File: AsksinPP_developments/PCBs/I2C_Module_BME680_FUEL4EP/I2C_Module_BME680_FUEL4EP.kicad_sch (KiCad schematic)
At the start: 12 parts, among them J1 Conn_01x04, J2 Conn_01x04, U1 BME680

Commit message: PCBs: I2C_Module_BME280_FUEL4EP and I2C_Module_BME680_FUEL4EP: updated LCSC numberss for assembly at JLCPCB
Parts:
- C1: LCSC (none) -> C19666; TYPE (none) -> 0603
- C3, C4: LCSC (none) -> C14663; TYPE (none) -> 0603
- R1, R2: LCSC (none) -> C25900; TYPE (none) -> 0402
- R3: LCSC (none) -> C25744; TYPE (none) -> 0402
- U1: LCSC (none) -> C125972; TYPE (none) -> LGA-8
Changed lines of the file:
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@@
       (effects (font (size 1.27 1.27)) hide)
+    )
+    (property "LCSC" "C25900" (id 4) (at 147.955 123.19 0)
+      (effects (font (size 1.27 1.27)) hide)
+    )
+    (property "TYPE" "0402" (id 5) (at 151.765 120.65 0)
+      (effects (font (size 1.524 1.524)) hide)
     )
     (pin "1")
@@
       (effects (font (size 1.27 1.27)) hide)
     )
+    (property "LCSC" "C14663" (id 4) (at 132.715 56.515 0)
+      (effects (font (size 1.27 1.27)) hide)
+    )
+    (property "TYPE" "0603" (id 5) (at 137.795 54.61 0)
+      (effects (font (size 1.524 1.524)) hide)
+    )
     (pin "1")
     (pin "2")
@@
     (property "Datasheet" "~" (id 3) (at 173.355 55.88 0)
       (effects (font (size 1.27 1.27)) hide)
+    )
+    (property "LCSC" "C25744" (id 4) (at 169.545 59.69 0)
+      (effects (font (size 1.27 1.27)) hide)
+    )
+    (property "TYPE" "0402" (id 5) (at 173.355 55.88 0)
+      (effects (font (size 1.524 1.524)) hide)
     )
     (pin "1")
@@
       (effects (font (size 1.27 1.27)) hide)
     )
+    (property "LCSC" "C19666" (id 4) (at 75.438 128.27 0)
+      (effects (font (size 1.27 1.27)) hide)
+    )
+    (property "TYPE" "0603" (id 5) (at 79.375 130.175 90)
+      (effects (font (size 1.524 1.524)) hide)
+    )
     (pin "1")
     (pin "2")
@@
     (property "Datasheet" "~" (id 3) (at 121.285 54.61 0)
       (effects (font (size 1.27 1.27)) hide)
+    )
+    (property "LCSC" "C14663" (id 4) (at 116.205 56.515 0)
+      (effects (font (size 1.27 1.27)) hide)
+    )
+    (property "TYPE" "0603" (id 5) (at 121.285 54.61 0)
+      (effects (font (size 1.524 1.524)) hide)
     )
     (pin "1")
@@
     (property "Datasheet" "https://ae-bst.resource.bosch.com/media/_tech/media/datasheets/BST-BME680-DS001.pdf" (id 3) (at 130.175 87.63 0)
       (effects (font (size 1.27 1.27)) hide)
+    )
+    (property "LCSC" "C125972" (id 4) (at 130.175 82.55 0)
+      (effects (font (size 1.524 1.524)) hide)
+    )
+    (property "TYPE" "LGA-8" (id 5) (at 130.175 82.55 0)
+      (effects (font (size 1.524 1.524)) hide)
     )
     (pin "1")
@@
       (effects (font (size 1.27 1.27)) hide)
     )
-    (pin "1")
+    (property "LCSC" "C25900" (id 4) (at 154.305 123.19 0)
+      (effects (font (size 1.27 1.27)) hide)
+    )
+    (property "TYPE" "0402" (id 5) (at 158.115 120.65 0)
+      (effects (font (size 1.524 1.524)) hide)
+    )
+    (pin "1")

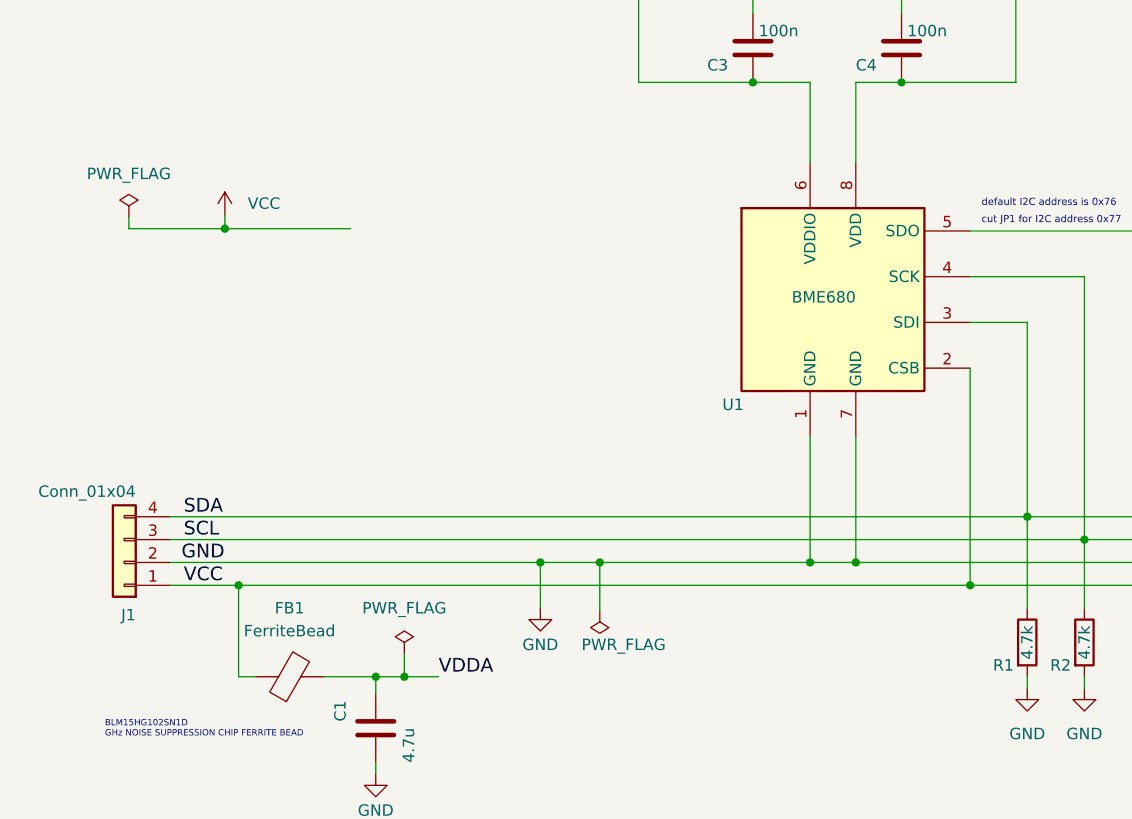
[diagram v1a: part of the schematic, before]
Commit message: PCBs: fix of some project specific KiCAD library paths for portability and missing PWR_FLGs for VCC in some schematics
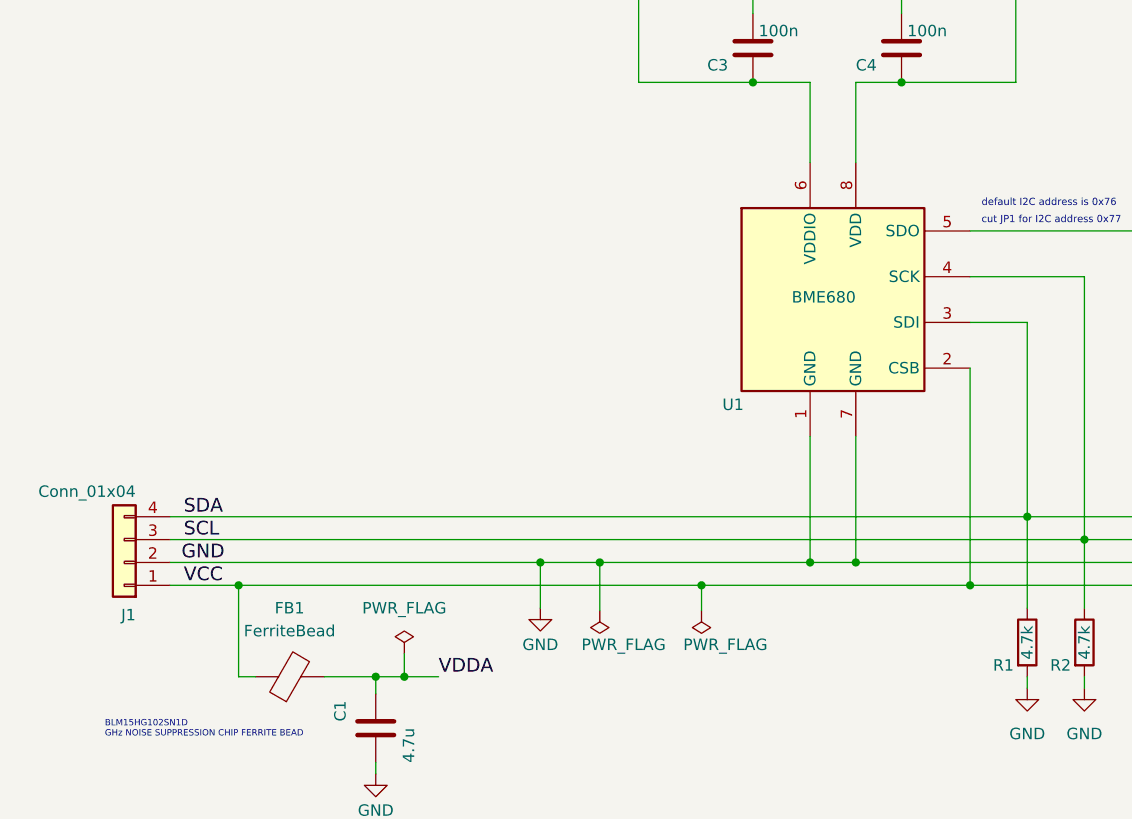
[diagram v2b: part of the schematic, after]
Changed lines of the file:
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@@
   (title_block
     (title "I2C_Module_BME680_FUEL4EP")
-    (date "2023-09-07")
-    (rev "1.0")
+    (date "2024-01-14")
+    (rev "1.1")
     (company "FUEL4EP")
     (comment 1 "fitting to  HB-UNI-SEN-BATT_ATMega1284P_E07-868MS10_FUEL4EP")
@@
   (junction (at 132.715 111.76) (diameter 0) (color 0 0 0 0)
   )
-  (junction (at 62.611 74.676) (diameter 0) (color 0 0 0 0)
-  )
   (junction (at 137.795 58.42) (diameter 0) (color 0 0 0 0)
   )
@@
   (junction (at 82.55 124.46) (diameter 0) (color 0 0 0 0)
   )
+  (junction (at 115.57 114.3) (diameter 0) (color 0 0 0 0)
+  )
   (junction (at 173.355 74.93) (diameter 0) (color 0 0 0 0)
   )
@@
     (stroke (width 0) (type default) (color 0 0 0 0))
   )
-  (wire (pts (xy 51.943 74.676) (xy 51.943 73.406))
-    (stroke (width 0) (type default) (color 0 0 0 0))
-  )
   (wire (pts (xy 121.285 48.26) (xy 121.285 50.8))
     (stroke (width 0) (type default) (color 0 0 0 0))
@@
     (stroke (width 0) (type default) (color 0 0 0 0))
   )
-  (wire (pts (xy 62.611 74.676) (xy 51.943 74.676))
-    (stroke (width 0) (type default) (color 0 0 0 0))
-  )
   (wire (pts (xy 145.415 80.01) (xy 158.115 80.01))
     (stroke (width 0) (type default) (color 0 0 0 0))
@@
     (stroke (width 0) (type default) (color 0 0 0 0))
   )
+  (wire (pts (xy 115.57 114.3) (xy 115.57 117.094))
+    (stroke (width 0) (type default) (color 0 0 0 0))
+  )
   (wire (pts (xy 79.375 124.46) (xy 79.375 126.365))
     (stroke (width 0) (type default) (color 0 0 0 0))
@@
     (stroke (width 0) (type default) (color 0 0 0 0))
   )
-  (wire (pts (xy 62.611 74.676) (xy 62.611 73.152))
-    (stroke (width 0) (type default) (color 0 0 0 0))
-  )
   (wire (pts (xy 108.585 58.42) (xy 121.285 58.42))
     (stroke (width 0) (type default) (color 0 0 0 0))
   )
-  (wire (pts (xy 64.135 114.3) (xy 145.415 114.3))
+  (wire (pts (xy 64.135 114.3) (xy 115.57 114.3))
     (stroke (width 0) (type default) (color 0 0 0 0))
   )
@@
     (stroke (width 0) (type default) (color 0 0 0 0))
   )
-  (wire (pts (xy 62.611 74.676) (xy 76.581 74.676))
-    (stroke (width 0) (type default) (color 0 0 0 0))
-  )
   (wire (pts (xy 56.515 111.76) (xy 97.663 111.76))
     (stroke (width 0) (type default) (color 0 0 0 0))
   )
   (wire (pts (xy 104.267 111.76) (xy 127.635 111.76))
+    (stroke (width 0) (type default) (color 0 0 0 0))
+  )
+  (wire (pts (xy 115.57 114.3) (xy 145.415 114.3))
     (stroke (width 0) (type default) (color 0 0 0 0))
   )
@@
     (pin "1")
   )
+  (symbol (lib_id "power:PWR_FLAG") (at 115.57 117.094 180) (unit 1)
+    (in_bom yes) (on_board yes)
+    (property "Reference" "#FLG0102" (id 0) (at 115.57 118.999 0)
+      (effects (font (size 1.27 1.27)) hide)
+    )
+    (property "Value" "PWR_FLAG" (id 1) (at 113.538 120.904 0)
+      (effects (font (size 1.27 1.27)) (justify right))
+    )
+    (property "Footprint" "" (id 2) (at 115.57 117.094 0)
+      (effects (font (size 1.27 1.27)) hide)
+    )
+    (property "Datasheet" "~" (id 3) (at 115.57 117.094 0)
+      (effects (font (size 1.27 1.27)) hide)
+    )
+    (pin "1")
+  )
   (symbol (lib_id "Device:R") (at 173.355 55.88 0) (unit 1)
     (in_bom yes) (on_board yes)
@@
     (pin "1")
     (pin "2")
-  )
-  (symbol (lib_id "power:VCC") (at 62.611 73.152 0) (unit 1)
-    (in_bom yes) (on_board yes) (fields_autoplaced)
-    (property "Reference" "#PWR01" (id 0) (at 62.611 76.962 0)
-      (effects (font (size 1.27 1.27)) hide)
-    )
-    (property "Value" "VCC" (id 1) (at 65.151 71.8819 0)
-      (effects (font (size 1.27 1.27)) (justify left))
-    )
-    (property "Footprint" "" (id 2) (at 62.611 73.152 0)
-      (effects (font (size 1.27 1.27)) hide)
-    )
-    (property "Datasheet" "" (id 3) (at 62.611 73.152 0)
-      (effects (font (size 1.27 1.27)) hide)
-    )
-    (pin "1")
   )
   (symbol (lib_id "Device:C") (at 79.375 130.175 0) (unit 1)
@@
     )
     (property "Datasheet" "" (id 3) (at 79.375 135.255 0)
-      (effects (font (size 1.27 1.27)) hide)
-    )
-    (pin "1")
-  )
-  (symbol (lib_id "power:PWR_FLAG") (at 51.943 73.406 0) (unit 1)
-    (in_bom yes) (on_board yes) (fields_autoplaced)
-    (property "Reference" "#FLG01" (id 0) (at 51.943 71.501 0)
-      (effects (font (size 1.27 1.27)) hide)
-    )
-    (property "Value" "PWR_FLAG" (id 1) (at 51.943 68.58 0))
-    (property "Footprint" "" (id 2) (at 51.943 73.406 0)
-      (effects (font (size 1.27 1.27)) hide)
-    )
-    (property "Datasheet" "~" (id 3) (at 51.943 73.406 0)
       (effects (font (size 1.27 1.27)) hide)
     )
@@
   )
   (symbol_instances
-    (path "/accbd0c3-e588-4a03-8c25-5dc64064deb9"
-      (reference "#FLG01") (unit 1) (value "PWR_FLAG") (footprint "")
-    )
     (path "/b998681a-aa50-4b75-bf22-d9fbe42fce6f"
       (reference "#FLG02") (unit 1) (value "PWR_FLAG") (footprint "")
@@
       (reference "#FLG0101") (unit 1) (value "PWR_FLAG") (footprint "")
     )
-    (path "/71fc455e-be46-44e1-9ad6-6659dc653656"
-      (reference "#PWR01") (unit 1) (value "VCC") (footprint "")
+    (path "/538d4725-6508-47aa-bf0f-3fed7444df70"
+      (reference "#FLG0102") (unit 1) (value "PWR_FLAG") (footprint "")
     )
     (path "/2fb280af-9352-43f7-93d8-89326fb5dc6f"

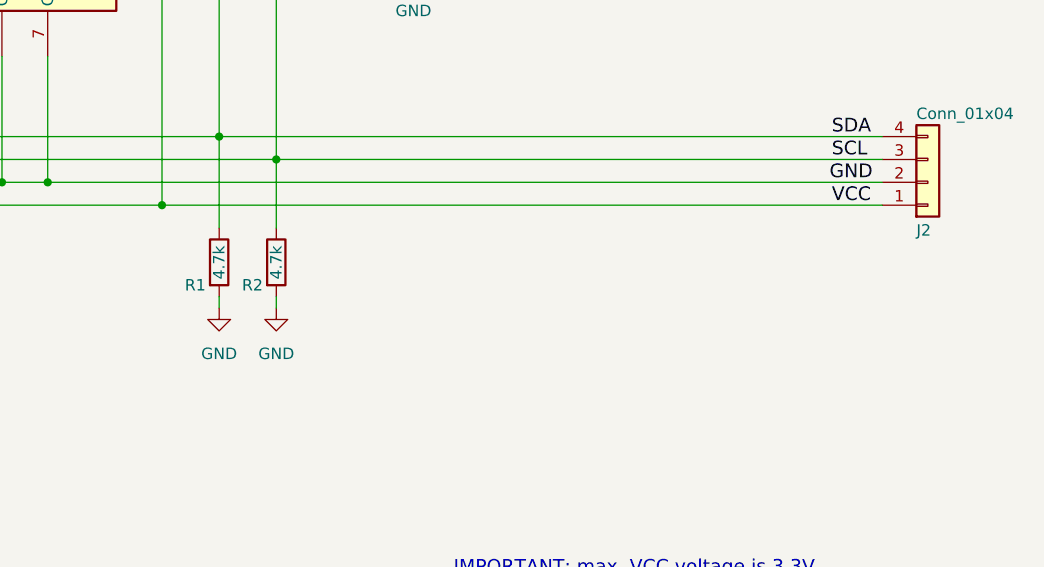
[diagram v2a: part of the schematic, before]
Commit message: PCBs: fix of I2C Pull-up resistors that were wrongly tied to GND
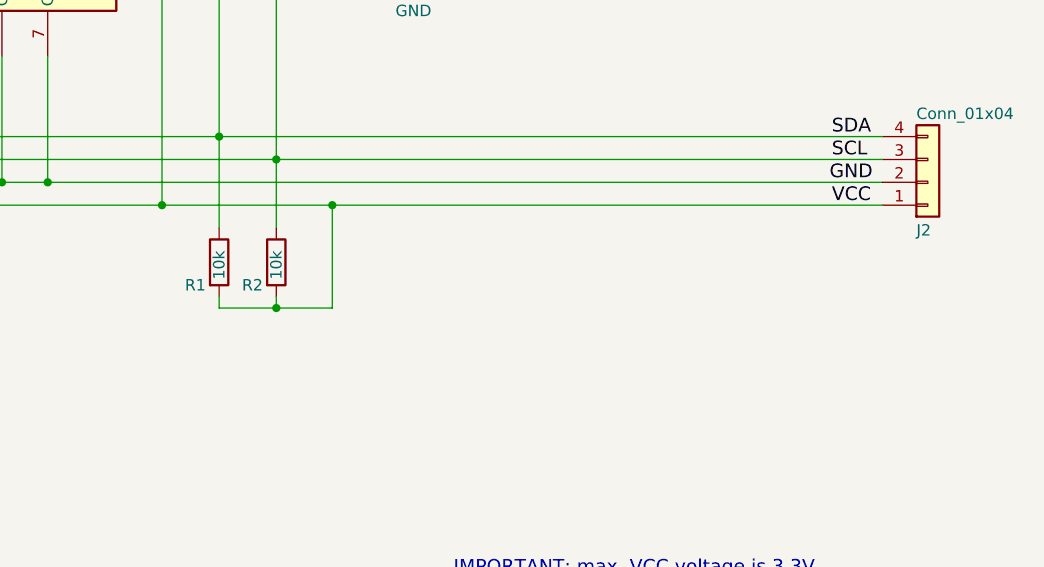
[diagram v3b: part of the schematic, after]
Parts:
- R1, R2: value 4.7k -> 10k; LCSC C25900 -> C25744
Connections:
- net GND: no longer R1.2, R2.2
- net VCC: now also R1.2, R2.2
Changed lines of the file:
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@@
   (title_block
     (title "I2C_Module_BME680_FUEL4EP")
-    (date "2024-01-14")
-    (rev "1.1")
+    (date "2024-02-08")
+    (rev "1.2")
     (company "FUEL4EP")
     (comment 1 "fitting to  HB-UNI-SEN-BATT_ATMega1284P_E07-868MS10_FUEL4EP")
@@
   (junction (at 137.795 58.42) (diameter 0) (color 0 0 0 0)
   )
+  (junction (at 164.338 114.3) (diameter 0) (color 0 0 0 0)
+  )
   (junction (at 79.375 124.46) (diameter 0) (color 0 0 0 0)
   )
   (junction (at 121.285 58.42) (diameter 0) (color 0 0 0 0)
   )
+  (junction (at 158.115 125.73) (diameter 0) (color 0 0 0 0)
+  )
   (junction (at 97.663 111.76) (diameter 0) (color 0 0 0 0)
   )
@@
     (stroke (width 0) (type default) (color 0 0 0 0))
   )
+  (wire (pts (xy 132.715 58.42) (xy 137.795 58.42))
+    (stroke (width 0) (type default) (color 0 0 0 0))
+  )
+  (wire (pts (xy 86.36 124.46) (xy 82.55 124.46))
+    (stroke (width 0) (type default) (color 0 0 0 0))
+  )
+  (wire (pts (xy 97.663 111.76) (xy 97.663 116.84))
+    (stroke (width 0) (type default) (color 0 0 0 0))
+  )
+  (wire (pts (xy 150.495 48.26) (xy 150.495 58.42))
+    (stroke (width 0) (type default) (color 0 0 0 0))
+  )
+  (wire (pts (xy 151.765 106.68) (xy 225.425 106.68))
+    (stroke (width 0) (type default) (color 0 0 0 0))
+  )
   (wire (pts (xy 158.115 124.46) (xy 158.115 125.73))
     (stroke (width 0) (type default) (color 0 0 0 0))
   )
-  (wire (pts (xy 132.715 58.42) (xy 137.795 58.42))
-    (stroke (width 0) (type default) (color 0 0 0 0))
-  )
-  (wire (pts (xy 86.36 124.46) (xy 82.55 124.46))
-    (stroke (width 0) (type default) (color 0 0 0 0))
-  )
-  (wire (pts (xy 97.663 111.76) (xy 97.663 116.84))
-    (stroke (width 0) (type default) (color 0 0 0 0))
-  )
-  (wire (pts (xy 150.495 48.26) (xy 150.495 58.42))
-    (stroke (width 0) (type default) (color 0 0 0 0))
-  )
-  (wire (pts (xy 151.765 106.68) (xy 225.425 106.68))
-    (stroke (width 0) (type default) (color 0 0 0 0))
-  )
   (wire (pts (xy 145.415 80.01) (xy 158.115 80.01))
     (stroke (width 0) (type default) (color 0 0 0 0))
@@
     (stroke (width 0) (type default) (color 0 0 0 0))
   )
+  (wire (pts (xy 164.338 125.73) (xy 164.338 114.3))
+    (stroke (width 0) (type default) (color 0 0 0 0))
+  )
   (wire (pts (xy 79.375 133.985) (xy 79.375 135.255))
     (stroke (width 0) (type default) (color 0 0 0 0))
@@
     (stroke (width 0) (type default) (color 0 0 0 0))
   )
+  (wire (pts (xy 158.115 125.73) (xy 164.338 125.73))
+    (stroke (width 0) (type default) (color 0 0 0 0))
+  )
   (wire (pts (xy 82.55 124.46) (xy 79.375 124.46))
     (stroke (width 0) (type default) (color 0 0 0 0))
@@
     (stroke (width 0) (type default) (color 0 0 0 0))
   )
+  (wire (pts (xy 151.765 125.73) (xy 158.115 125.73))
+    (stroke (width 0) (type default) (color 0 0 0 0))
+  )
   (wire (pts (xy 82.55 121.92) (xy 82.55 124.46))
     (stroke (width 0) (type default) (color 0 0 0 0))
@@
     (stroke (width 0) (type default) (color 0 0 0 0))
   )
+  (wire (pts (xy 164.338 114.3) (xy 225.425 114.3))
+    (stroke (width 0) (type default) (color 0 0 0 0))
+  )
   (wire (pts (xy 64.135 114.3) (xy 64.135 124.46))
     (stroke (width 0) (type default) (color 0 0 0 0))
   )
-  (wire (pts (xy 145.415 114.3) (xy 225.425 114.3))
+  (wire (pts (xy 145.415 114.3) (xy 164.338 114.3))
     (stroke (width 0) (type default) (color 0 0 0 0))
   )
@@
       (effects (font (size 1.27 1.27)) (justify left))
     )
-    (property "Value" "4.7k" (id 1) (at 151.765 122.555 90)
+    (property "Value" "10k" (id 1) (at 151.765 122.555 90)
       (effects (font (size 1.27 1.27)) (justify left))
     )
@@
       (effects (font (size 1.27 1.27)) hide)
     )
-    (property "LCSC" "C25900" (id 4) (at 147.955 123.19 0)
+    (property "LCSC" "C25744" (id 4) (at 147.955 123.19 0)
       (effects (font (size 1.27 1.27)) hide)
     )
@@
     )
     (property "Datasheet" "" (id 3) (at 121.285 48.26 0)
-      (effects (font (size 1.27 1.27)) hide)
-    )
-    (pin "1")
-  )
-  (symbol (lib_id "power:GND") (at 151.765 125.73 0) (unit 1)
-    (in_bom yes) (on_board yes) (fields_autoplaced)
-    (property "Reference" "#PWR07" (id 0) (at 151.765 132.08 0)
-      (effects (font (size 1.27 1.27)) hide)
-    )
-    (property "Value" "GND" (id 1) (at 151.765 130.81 0))
-    (property "Footprint" "" (id 2) (at 151.765 125.73 0)
-      (effects (font (size 1.27 1.27)) hide)
-    )
-    (property "Datasheet" "" (id 3) (at 151.765 125.73 0)
       (effects (font (size 1.27 1.27)) hide)
     )
@@
     (pin "8")
   )
-  (symbol (lib_id "power:GND") (at 158.115 125.73 0) (unit 1)
-    (in_bom yes) (on_board yes) (fields_autoplaced)
-    (property "Reference" "#PWR08" (id 0) (at 158.115 132.08 0)
-      (effects (font (size 1.27 1.27)) hide)
-    )
-    (property "Value" "GND" (id 1) (at 158.115 130.81 0))
-    (property "Footprint" "" (id 2) (at 158.115 125.73 0)
-      (effects (font (size 1.27 1.27)) hide)
-    )
-    (property "Datasheet" "" (id 3) (at 158.115 125.73 0)
-      (effects (font (size 1.27 1.27)) hide)
-    )
-    (pin "1")
-  )
   (symbol (lib_id "power:VDDA") (at 150.495 48.26 0) (unit 1)
     (in_bom yes) (on_board yes) (fields_autoplaced)
@@
       (effects (font (size 1.27 1.27)) (justify left))
     )
-    (property "Value" "4.7k" (id 1) (at 158.115 122.555 90)
+    (property "Value" "10k" (id 1) (at 158.115 122.555 90)
       (effects (font (size 1.27 1.27)) (justify left))
     )
@@
       (effects (font (size 1.27 1.27)) hide)
     )
-    (property "LCSC" "C25900" (id 4) (at 154.305 123.19 0)
+    (property "LCSC" "C25744" (id 4) (at 154.305 123.19 0)
       (effects (font (size 1.27 1.27)) hide)
     )
@@
       (reference "#PWR05") (unit 1) (value "GND") (footprint "")
     )
-    (path "/18542ab6-239f-4332-a70c-3c8551b285bb"
-      (reference "#PWR07") (unit 1) (value "GND") (footprint "")
-    )
-    (path "/d43541cc-8fb7-4c57-a7c8-5b5588c55acf"
-      (reference "#PWR08") (unit 1) (value "GND") (footprint "")
-    )
     (path "/3c4dcae3-942c-4516-aa17-b3223b1ea5e6"
       (reference "#PWR010") (unit 1) (value "GND") (footprint "")
@@
     )
     (path "/010452d5-e5f2-447e-a153-71da0dbec114"
-      (reference "R1") (unit 1) (value "4.7k") (footprint "Resistor_SMD:R_0402_1005Metric")
+      (reference "R1") (unit 1) (value "10k") (footprint "Resistor_SMD:R_0402_1005Metric")
     )
     (path "/f75dc7be-70bf-4119-8c06-195e1a960dd2"
-      (reference "R2") (unit 1) (value "4.7k") (footprint "Resistor_SMD:R_0402_1005Metric")
+      (reference "R2") (unit 1) (value "10k") (footprint "Resistor_SMD:R_0402_1005Metric")
     )
     (path "/55b96afd-ec19-4400-9134-cc56302d872a"
